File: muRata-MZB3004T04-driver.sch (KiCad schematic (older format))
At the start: 33 parts, among them IC1 OPA4191, Q1 MOS_RM4606S8, Q2 Trans_PBSS4032SPN, Q3 Trans_2ct_NPN_PNP_PBSS4032SPN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

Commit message: Rename 'Vin' to 'Vm'
The designator was taken from the MZB3004T04 datasheet, but
due to low image fidelity, it was hard to tell exactly what
character(s) followed the 'V' for this particular label.

It has occurred to me, of course, that 'Vin' might be a very confusing
interpretation. After all, this is not the input voltage for the board.
That voltage is 'Vs', presumably "voltage source". Given the
resistor-divider circuit that produces 'Vm'/'Vin', I suspect
that this is a half-voltage, so "voltage mid" or "voltage middle"
might be a less confusing interpretation, hence 'Vm'.
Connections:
- net Vin renamed Vm
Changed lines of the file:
@@
 GND
 Text GLabel 1850 6250 2    50   Output ~ 0
-Vin
+Vm
 Wire Wire Line
 	1000 5700 1000 5550
@@
 $EndComp
 Text GLabel 2850 6400 3    50   Input ~ 0
-Vin
+Vm
 $Comp
 L V_Passive:R R8
@@
 OPAM
 Text GLabel 5100 6350 0    50   Input ~ 0
-Vin
+Vm
 Text GLabel 5100 6500 0    50   Input ~ 0
 Vc
 Text GLabel 5100 6650 0    50   Input ~ 0
-Vin
+Vm
 Text GLabel 5100 6800 0    50   Input ~ 0
 OPBM
@@
 OPDM
 Text GLabel 6400 6350 2    50   Input ~ 0
-Vin
+Vm
 Text GLabel 6400 6500 2    50   Input ~ 0
 GND
@@
 	8750 5650 8850 5650
 Text GLabel 8750 6250 3    50   Input ~ 0
-Vin
+Vm
 $Comp
 L V_Passive:R R14
@@
 $EndComp
 Text GLabel 8000 3050 1    50   Input ~ 0
-Vin
+Vm
 Wire Wire Line
 	7900 3750 8000 3750

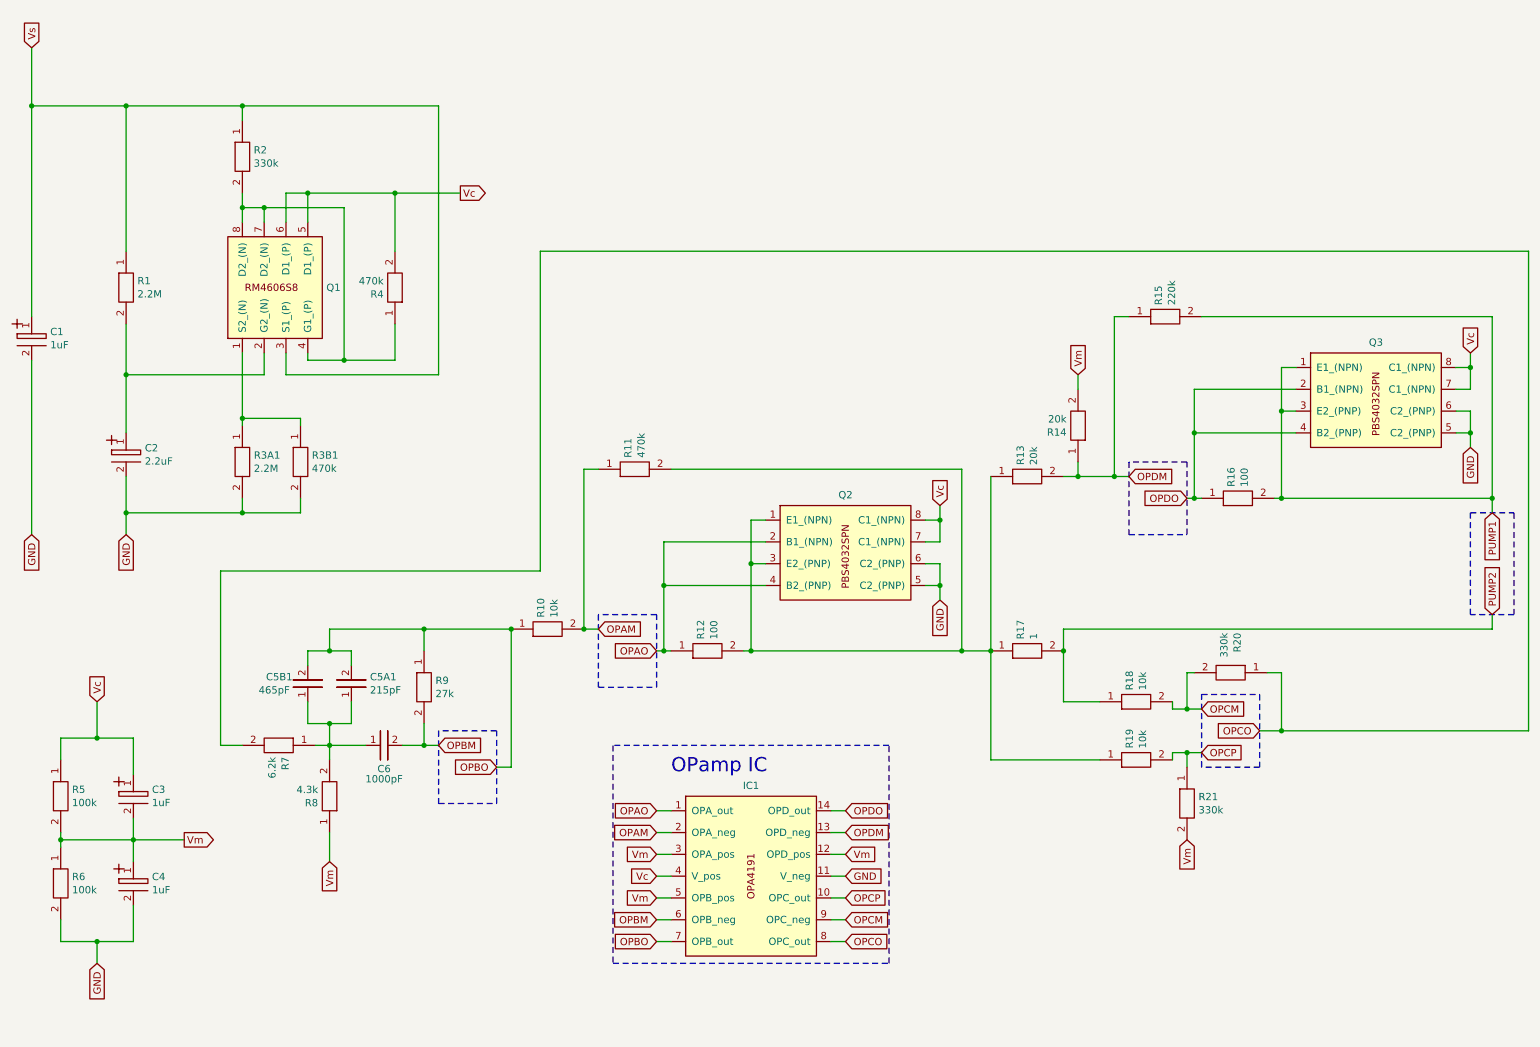
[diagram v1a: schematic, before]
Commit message: Add TTL switching MOSFET to design.
This allows the >8V power voltage `Vs` to be controlled by
a lower-voltage signal `Vsig` (3.3V in my case).
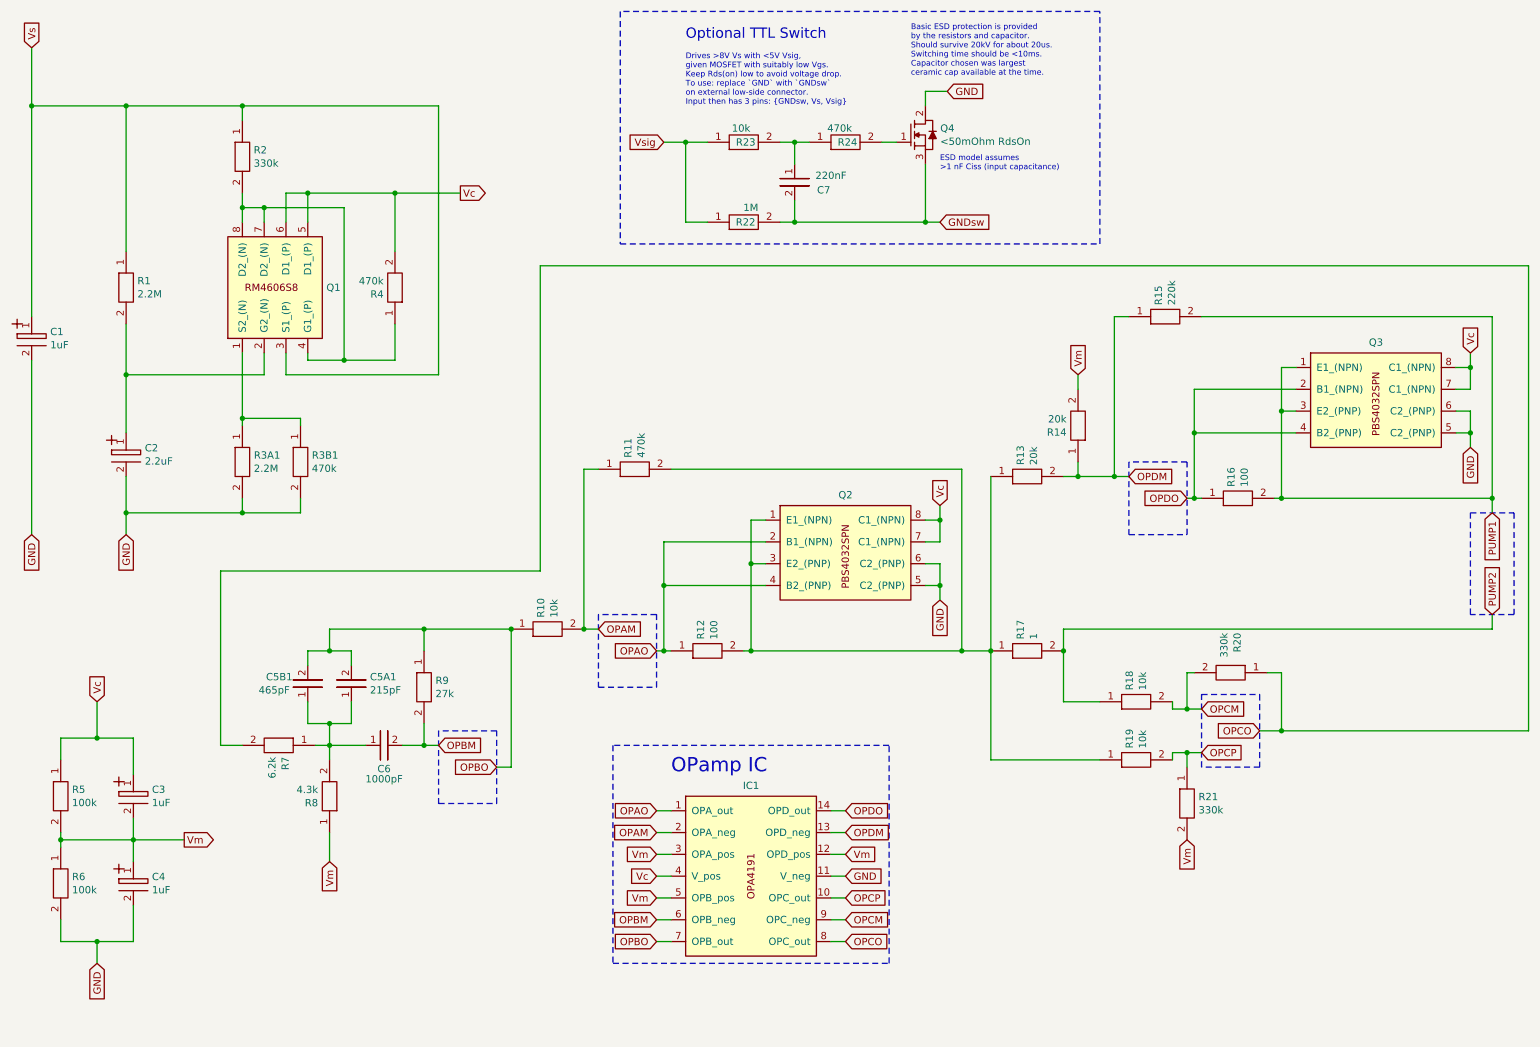
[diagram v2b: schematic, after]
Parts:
- added C7: 220nF, AX1_1N, symbol custom_ics:C-Ceramic_AX1_1N
- added Q4: <50mOhm RdsOn, MOSFET_1CT_L3x1, symbol custom_ics:MOSFET_1ct_Nch_Enh
- added R22: 1M, AX3_1, symbol V_Passive:R
- added R23: 10k, AX3_1, symbol V_Passive:R
- added R24: 470k, AX3_1, symbol V_Passive:R
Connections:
- net GND: now also Q4.2
- new net: Q4.1, R24.2
- new net: C7.1, R23.2, R24.1
- new net GNDsw: C7.2, Q4.3, R22.2
- new net Vsig: R22.1, R23.1
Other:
- note added: "Basic ESD protection is provided\nby the resistors and capacitor.\nShould survive 20kV for about 20us.\nSwitching time should be <10ms.\nCapacitor chosen was largest\nceramic cap available at the time."
- note added: "Drives >8V Vs with <5V Vsig,\ngiven MOSFET with suitably low Vgs.\nKeep Rds(on) low to avoid voltage drop.\nTo use: replace `GND` with `GNDsw`\non external low-side connector.\nInput then has 3 pins: {GNDsw, Vs, Vsig}"
- note added: "ESD model assumes\n>1 nF Ciss (input capacitance)"
- note added: "Optional TTL Switch"
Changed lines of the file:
@@
 Text GLabel 800  800  1    50   Input ~ 0
 Vs
-Text GLabel 1450 4150 3    50   Input ~ 0
-GND
 Text GLabel 800  4150 3    50   Input ~ 0
 GND
@@
 	1    0    0    -1
 $EndComp
-$Comp
-L V_Passive:R R1
-U 1 1 62D1A302
-P 1450 2450
-F 0 "R1" H 1528 2496 50  0000 L CNN
-F 1 "2.2M" H 1528 2405 50  0000 L CNN
-F 2 "AX3_1" H 1450 2450 50  0001 C CNN
-F 3 "" H 1450 2450 50  0001 C CNN
-	1    1450 2450
-	1    0    0    -1
-$EndComp
 Wire Wire Line
 	2650 3400 2650 3350
@@
 	2650 4000 2650 3900
 Wire Wire Line
-	2250 4000 1450 4000
-Connection ~ 2250 4000
-Wire Wire Line
-	1450 4000 1450 4150
-Wire Wire Line
 	2250 1900 2400 1900
 Wire Wire Line
@@
 	2550 3050 2550 2900
 Wire Wire Line
-	1450 2700 1450 3050
-Wire Wire Line
 	2400 2900 2400 3050
-Wire Wire Line
-	2400 3050 1450 3050
-Connection ~ 1450 3050
-Wire Wire Line
-	1450 3050 1450 3450
 Wire Wire Line
 	2550 2000 2550 1800
@@
 Connection ~ 2250 1900
 Wire Wire Line
-	800  800  800  1200
-Wire Wire Line
-	1450 2200 1450 1200
-Wire Wire Line
-	1450 1200 2250 1200
-Wire Wire Line
 	2250 1200 2250 1300
-Wire Wire Line
-	1450 1200 800  1200
-Connection ~ 1450 1200
-Connection ~ 800  1200
-Wire Wire Line
-	800  1200 800  2650
 Connection ~ 2250 1200
 Wire Wire Line
@@
 Wire Wire Line
 	800  2950 800  4150
-Wire Wire Line
-	1450 3750 1450 4000
-Connection ~ 1450 4000
 $Comp
 L V_Passive:R R5
@@
 F 3 "" H 750 2800 50  0001 C CNN
 	1    750  2800
-	-1   0    0    1
-$EndComp
-$Comp
-L V_Passive:C-ELECTRO_RA1_3 C2
-U 1 1 62D2E23E
-P 1400 3600
-F 0 "C2" H 1221 3554 50  0000 R CNN
-F 1 "2.2uF" H 1221 3645 50  0000 R CNN
-F 2 "RA1_3" H 1400 3600 50  0001 C CNN
-F 3 "" H 1400 3600 50  0001 C CNN
-	1    1400 3600
 	-1   0    0    1
 $EndComp
@@
 	2100 4400 4300 4400
 Wire Wire Line
-	4300 4400 4300 2200
-Wire Wire Line
-	4300 2200 11100 2200
-Wire Wire Line
-	11100 2200 11100 5500
-Wire Wire Line
 	11100 5500 9400 5500
 Connection ~ 9400 5500
@@
 	-1   0    0    1
 $EndComp
+Wire Wire Line
+	800  800  800  1200
+Connection ~ 800  1200
+Connection ~ 2250 4000
+Wire Wire Line
+	2250 4000 1450 4000
+Wire Wire Line
+	1450 3750 1450 4000
+Connection ~ 1450 4000
+Wire Wire Line
+	1450 4000 1450 4150
+Text GLabel 1450 4150 3    50   Input ~ 0
+GND
+Wire Wire Line
+	1450 3050 1450 3450
+$Comp
+L V_Passive:C-ELECTRO_RA1_3 C2
+U 1 1 62D2E23E
+P 1400 3600
+F 0 "C2" H 1221 3554 50  0000 R CNN
+F 1 "2.2uF" H 1221 3645 50  0000 R CNN
+F 2 "RA1_3" H 1400 3600 50  0001 C CNN
+F 3 "" H 1400 3600 50  0001 C CNN
+	1    1400 3600
+	-1   0    0    1
+$EndComp
+Wire Wire Line
+	2400 3050 1450 3050
+Wire Wire Line
+	800  1200 800  2650
+Wire Wire Line
+	1450 1200 800  1200
+Wire Wire Line
+	1450 1200 2250 1200
+Connection ~ 1450 1200
+Wire Wire Line
+	1450 2200 1450 1200
+$Comp
+L V_Passive:R R1
+U 1 1 62D1A302
+P 1450 2450
+F 0 "R1" H 1528 2496 50  0000 L CNN
+F 1 "2.2M" H 1528 2405 50  0000 L CNN
+F 2 "AX3_1" H 1450 2450 50  0001 C CNN
+F 3 "" H 1450 2450 50  0001 C CNN
+	1    1450 2450
+	1    0    0    -1
+$EndComp
+Connection ~ 1450 3050
+Wire Wire Line
+	1450 2700 1450 3050
+Text Notes 5300 750  0    71   ~ 0
+Optional TTL Switch
+Text Notes 5300 1200 0    39   ~ 0
+Drives >8V Vs with <5V Vsig,\ngiven MOSFET with suitably low Vgs.\nKeep Rds(on) low to avoid voltage drop.\nTo use: replace `GND` with `GNDsw`\non external low-side connector.\nInput then has 3 pins: {GNDsw, Vs, Vsig}
+Wire Wire Line
+	11100 5500 11100 2300
+Wire Wire Line
+	11100 2300 4300 2300
+Wire Wire Line
+	4300 2300 4300 4400
+Wire Wire Line
+	6950 1100 7100 1100
+Wire Wire Line
+	6950 2000 7050 2000
+Wire Wire Line
+	6950 1200 6950 1100
+Text GLabel 5150 1450 0    50   Input ~ 0
+Vsig
+Text GLabel 7050 2000 2    50   Input ~ 0
+GNDsw
+Text GLabel 7100 1100 2    50   Input ~ 0
+GND
+Wire Wire Line
+	6950 1600 6950 2000
+Wire Wire Line
+	5150 1450 5300 1450
+Wire Wire Line
+	5300 1450 5300 2000
+Wire Wire Line
+	5300 2000 5450 2000
+Connection ~ 5300 1450
+Wire Wire Line
+	5300 1450 5450 1450
+Connection ~ 6950 2000
+Wire Wire Line
+	6650 1450 6750 1450
+$Comp
+L V_Passive:R R23
+U 1 1 62EDE748
+P 5700 1450
+F 0 "R23" V 5700 1369 50  0000 L CNN
+F 1 "10k" V 5796 1405 50  0000 L CNN
+F 2 "AX3_1" H 5700 1450 50  0001 C CNN
+F 3 "" H 5700 1450 50  0001 C CNN
+	1    5700 1450
+	0    -1   -1   0
+$EndComp
+$Comp
+L V_Passive:R R22
+U 1 1 62D54DDC
+P 5700 2000
+F 0 "R22" V 5700 1920 50  0000 L CNN
+F 1 "1M" V 5800 1900 50  0000 L CNN
+F 2 "AX3_1" H 5700 2000 50  0001 C CNN
+F 3 "" H 5700 2000 50  0001 C CNN
+	1    5700 2000
+	0    -1   -1   0
+$EndComp
+$Comp
+L custom_ics:C-Ceramic_AX1_1N C7
+U 1 1 62FC70E2
+P 6050 1700
+F 0 "C7" H 5850 1750 50  0000 C BNN
+F 1 "220nF" H 5800 1650 50  0000 C BNN
+F 2 "AX1_1N" H 5750 1900 50  0001 C CNN
+F 3 "" H 5750 1900 50  0001 C CNN
+	1    6050 1700
+	-1   0    0    1
+$EndComp
+$Comp
+L V_Passive:R R24
+U 1 1 62FE2B5E
+P 6400 1450
+F 0 "R24" V 6400 1369 50  0000 L CNN
+F 1 "470k" V 6496 1405 50  0000 L CNN
+F 2 "AX3_1" H 6400 1450 50  0001 C CNN
+F 3 "" H 6400 1450 50  0001 C CNN
+	1    6400 1450
+	0    -1   -1   0
+$EndComp
+Wire Wire Line
+	5950 2000 6050 2000
+Wire Wire Line
+	6050 1850 6050 2000
+Connection ~ 6050 2000
+Wire Wire Line
+	6050 2000 6950 2000
+Wire Wire Line
+	5950 1450 6050 1450
+Wire Wire Line
+	6050 1450 6050 1600
+Wire Wire Line
+	6050 1450 6150 1450
+Connection ~ 6050 1450
+$Comp
+L custom_ics:MOSFET_1ct_Nch_Enh Q4
+U 1 1 62D546CF
+P 6900 1400
+F 0 "Q4" H 7052 1446 50  0000 L CNN
+F 1 "<50mOhm RdsOn" H 7052 1355 50  0000 L CNN
+F 2 "MOSFET_1CT_L3x1" H 6900 1750 50  0001 C CNN
+F 3 "" H 6800 1550 50  0001 C CNN
+	1    6900 1400
+	1    0    0    -1
+$EndComp
+Text Notes 7050 1650 0    39   ~ 0
+ESD model assumes\n>1 nF Ciss (input capacitance)
+Text Notes 6850 1000 0    39   ~ 0
+Basic ESD protection is provided\nby the resistors and capacitor.\nShould survive 20kV for about 20us.\nSwitching time should be <10ms.\nCapacitor chosen was largest\nceramic cap available at the time.
+Wire Notes Line
+	4850 550  4850 2150
+Wire Notes Line
+	4850 2150 8150 2150
+Wire Notes Line
+	8150 2150 8150 550
+Wire Notes Line
+	8150 550  4850 550
 $EndSCHEMATC

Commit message: Add connector components to schematic+layout.
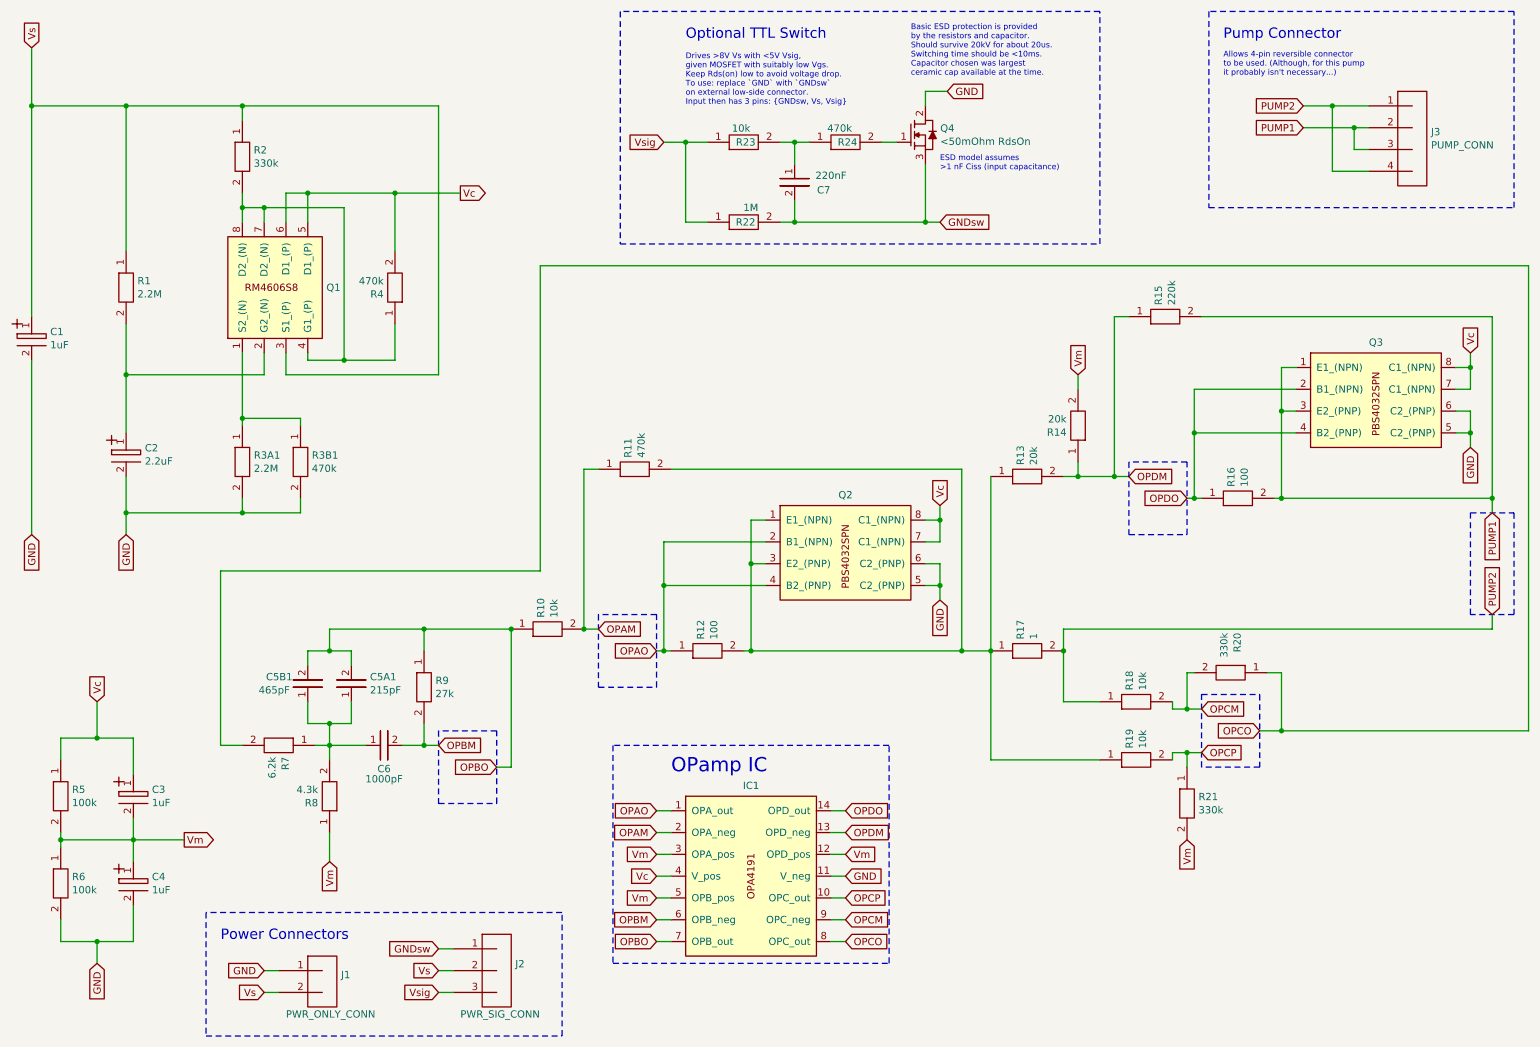
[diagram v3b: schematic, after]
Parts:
- added J1: PWR_ONLY_CONN, SIP2, symbol V_Connector:CONN_2
- added J2: PWR_SIG_CONN, SIP3, symbol V_Connector:CONN_3
- added J3: PUMP_CONN, SIP4, symbol V_Connector:CONN_4
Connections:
- net GND: now also J1.1
- net GNDsw: now also J2.1
- net PUMP1: now also J3.2, J3.3
- net PUMP2: now also J3.1, J3.4
- net Vs: now also J1.2, J2.2
- net Vsig: now also J2.3
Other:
- note added: "Allows 4-pin reversible connector\nto be used. (Although, for this pump\nit probably isn't necessary...)"
- note added: "Power Connectors"
- note added: "Pump Connector"
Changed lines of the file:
@@
 Wire Wire Line
 	10850 2650 10850 3900
-Wire Wire Line
-	10850 3900 9400 3900
 Connection ~ 9400 3900
-Wire Wire Line
-	10850 4800 7900 4800
-Wire Wire Line
-	7900 4800 7900 4950
 Connection ~ 7900 4950
-Text GLabel 10850 4700 1    50   Input ~ 0
-PUMP2
-Text GLabel 10850 4000 3    50   Input ~ 0
-PUMP1
-Wire Wire Line
-	10850 3900 10850 4000
-Connection ~ 10850 3900
-Wire Wire Line
-	10850 4800 10850 4700
-Wire Notes Line
-	10700 4000 11000 4000
-Wire Notes Line
-	11000 4000 11000 4700
-Wire Notes Line
-	11000 4700 10700 4700
-Wire Notes Line
-	10700 4700 10700 4000
 Wire Wire Line
 	2250 5600 2100 5600
@@
 Wire Notes Line
 	8150 550  4850 550
+Wire Wire Line
+	10850 3900 9400 3900
+Wire Wire Line
+	7900 4800 7900 4950
+Wire Wire Line
+	10850 4800 7900 4800
+Wire Wire Line
+	10850 4800 10850 4700
+Connection ~ 10850 3900
+Wire Wire Line
+	10850 3900 10850 4000
+$Comp
+L V_Connector:CONN_4 J3
+U 1 1 63059671
+P 10200 1450
+F 0 "J3" H 10429 1521 50  0000 L CNN
+F 1 "PUMP_CONN" H 10429 1430 50  0000 L CNN
+F 2 "SIP4" H 10200 1450 50  0001 C CNN
+F 3 "" H 10200 1450 50  0001 C CNN
+	1    10200 1450
+	1    0    0    -1
+$EndComp
+Wire Notes Line
+	11000 4000 11000 4700
+Wire Notes Line
+	10700 4000 11000 4000
+Wire Notes Line
+	11000 4700 10700 4700
+Wire Notes Line
+	10700 4700 10700 4000
+Text GLabel 10850 4000 3    50   Input ~ 0
+PUMP1
+Text GLabel 10850 4700 1    50   Input ~ 0
+PUMP2
+Wire Wire Line
+	9900 1350 9900 1500
+Wire Wire Line
+	9900 1500 10000 1500
+Wire Wire Line
+	9900 1350 10000 1350
+Wire Wire Line
+	9750 1200 9750 1650
+Wire Wire Line
+	9750 1650 10000 1650
+Wire Wire Line
+	9750 1200 10000 1200
+Text GLabel 9550 1200 0    50   Input ~ 0
+PUMP2
+Text GLabel 9550 1350 0    50   Input ~ 0
+PUMP1
+Wire Wire Line
+	9550 1200 9750 1200
+Connection ~ 9750 1200
+Wire Wire Line
+	9550 1350 9900 1350
+Connection ~ 9900 1350
+Text Notes 9000 750  0    71   ~ 0
+Pump Connector
+Text Notes 9000 1000 0    39   ~ 0
+Allows 4-pin reversible connector\nto be used. (Although, for this pump\nit probably isn't necessary...)
+Wire Notes Line
+	8900 550  8900 1900
+Wire Notes Line
+	8900 1900 11000 1900
+Wire Notes Line
+	11000 1900 11000 550
+Wire Notes Line
+	11000 550  8900 550
+$Comp
+L V_Connector:CONN_3 J2
+U 1 1 63150570
+P 3900 7150
+F 0 "J2" H 4128 7196 50  0000 L CNN
+F 1 "PWR_SIG_CONN" H 3750 6850 50  0000 L CNN
+F 2 "SIP3" H 3900 7150 50  0001 C CNN
+F 3 "" H 3900 7150 50  0001 C CNN
+	1    3900 7150
+	1    0    0    -1
+$EndComp
+$Comp
+L V_Connector:CONN_2 J1
+U 1 1 63151226
+P 2700 7250
+F 0 "J1" H 2929 7321 50  0000 L CNN
+F 1 "PWR_ONLY_CONN" H 2550 7050 50  0000 L CNN
+F 2 "SIP2" H 2700 7250 50  0001 C CNN
+F 3 "" H 2700 7250 50  0001 C CNN
+	1    2700 7250
+	1    0    0    -1
+$EndComp
+Text GLabel 2400 7150 0    50   Input ~ 0
+GND
+Text GLabel 2400 7300 0    50   Input ~ 0
+Vs
+Text GLabel 3600 7150 0    50   Input ~ 0
+Vs
+Text GLabel 3600 7000 0    50   Input ~ 0
+GNDsw
+Text GLabel 3600 7300 0    50   Input ~ 0
+Vsig
+Wire Wire Line
+	3600 7000 3700 7000
+Wire Wire Line
+	3600 7150 3700 7150
+Wire Wire Line
+	3600 7300 3700 7300
+Wire Wire Line
+	2400 7150 2500 7150
+Wire Wire Line
+	2400 7300 2500 7300
+Text Notes 2100 6950 0    71   ~ 0
+Power Connectors
+Wire Notes Line
+	2000 6750 2000 7600
+Wire Notes Line
+	2000 7600 4450 7600
+Wire Notes Line
+	4450 7600 4450 6750
+Wire Notes Line
+	4450 6750 2000 6750
 $EndSCHEMATC
